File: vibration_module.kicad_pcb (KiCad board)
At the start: 2 copper layers, 17.5 x 17 mm, 21 parts, among them J1 I2C/PWR, U1 AT42QT1011-TSHR, U2 DRV2605LDGS, U3 STM32G031G8Ux, U4 TPS7A20xxxDQN

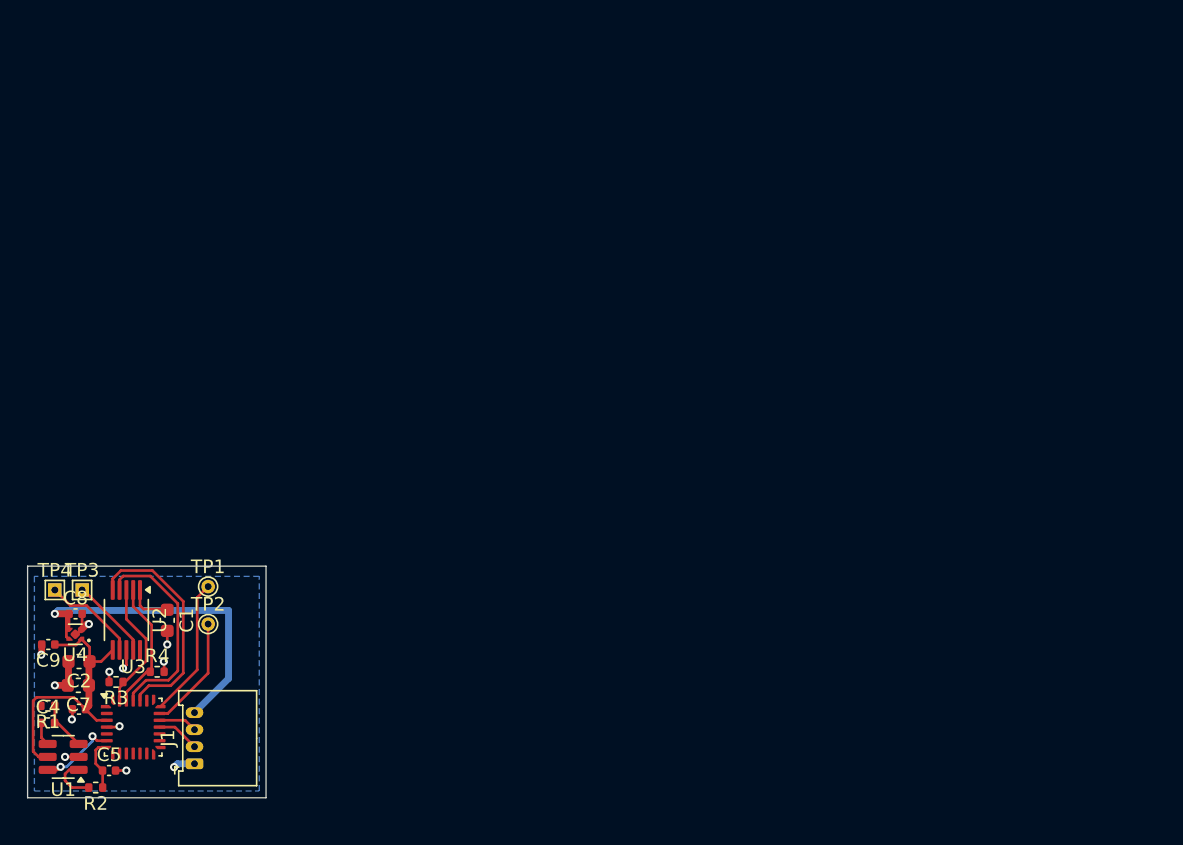
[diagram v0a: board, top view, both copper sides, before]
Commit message: mouse switch integration
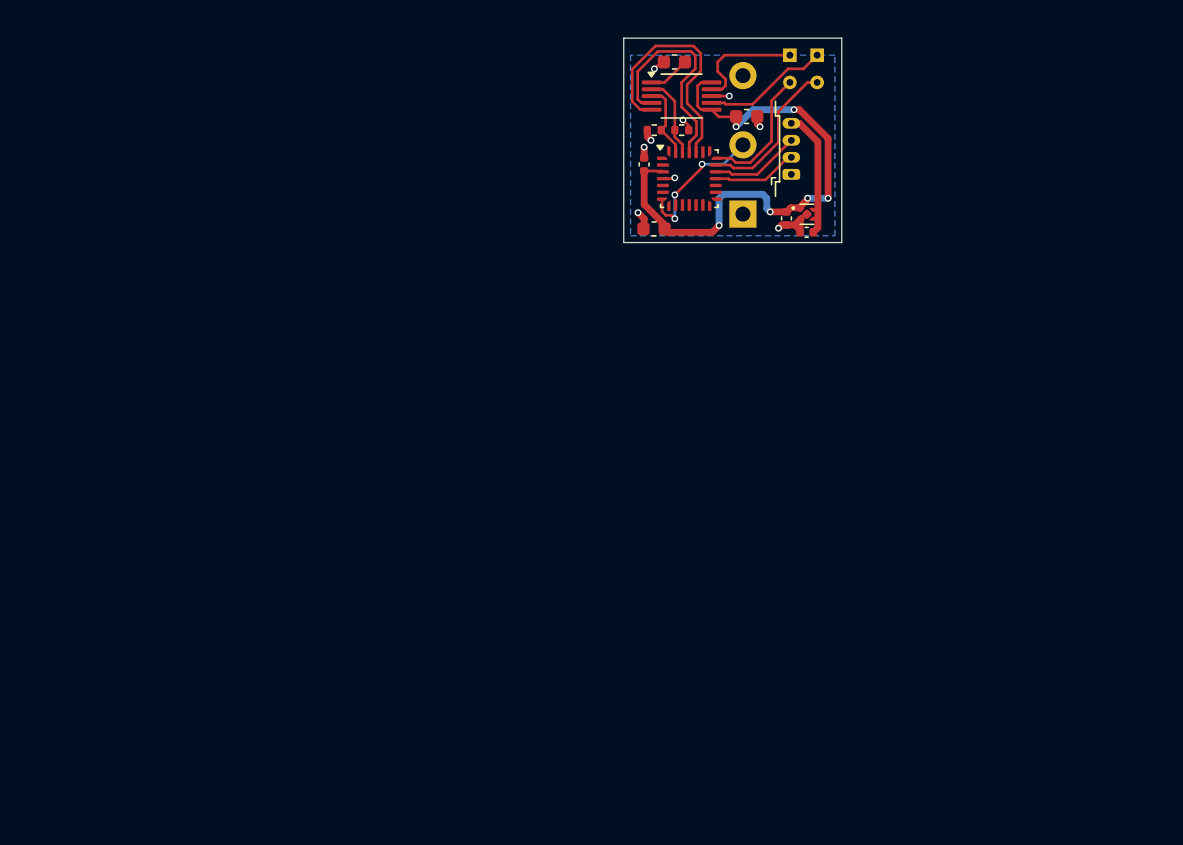
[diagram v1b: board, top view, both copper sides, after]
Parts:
- removed C4, C5: 10n, Capacitor_SMD:C_0402_1005Metric
- removed R1, R2: 10k, Resistor_SMD:R_0402_1005Metric
- removed U1: AT42QT1011-TSHR, Package_TO_SOT_SMD:SOT-23-6
- added SW1: SW_SPDT, Button_Switch_THT:SW_XKB_DM1-16UP-1, B.Cu at (163.2, 78.2)
- moved TP4 68.3 mm to (168.7, 66.5)
- moved TP3 65.1 mm to (166.7, 66.5)
- moved C2 63.3 mm to (163.5, 71.0), turned to 0 degrees
- moved C9 62.6 mm to (166.4, 78.5), turned to -90 degrees
- moved U4 61.9 mm to (167.9, 78.2), turned to 0 degrees
- moved J1 61.6 mm to (166.8, 75.2)
- moved C8 60.5 mm to (167.9, 79.5), turned to 180 degrees
- moved TP2 59.8 mm to (168.7, 68.5)
- moved C6 57.6 mm to (156.0, 74.5), turned to 90 degrees
- moved U3 57.3 mm to (159.3, 75.6)
- moved R3 56.6 mm to (156.7, 72.0)
- moved TP1 56.5 mm to (166.7, 68.5)
- moved U2 56.0 mm to (158.8, 69.5), turned to 0 degrees
- moved C1 55.4 mm to (158.2, 67.0), turned to 0 degrees
- moved R4 55.3 mm to (158.8, 72.0)
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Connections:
- U3 pad 6: Net-(U1-SYNC) -> unconnected-(U3-PA0-Pad6)
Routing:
- net +3.3V: track 21.2 -> 41.2 mm, vias 0 -> 6
- net VBUS: track 25.6 -> 8.91 mm, vias 1 -> 0
- net Net-(SW1-B): track 3.79 -> 10.5 mm, vias 0 -> 3
- net Net-(U1-SYNC): track 5.70 -> 0.00 mm, vias 2 -> 0
- net Net-(U2-SDA): track 9.53 -> 5.57 mm
- net /SDA: track 2.85 -> 6.66 mm
- net Net-(U1-SNSK): track 3.67 -> 0.00 mm
- net Net-(U1-OUT): track 3.57 -> 0.00 mm
- net Net-(U2-SCL): track 9.38 -> 6.05 mm
- net /SCL: track 3.16 -> 6.38 mm
- net Net-(U3-PA13): track 8.39 -> 11.6 mm
- net Net-(U2-OUT-): track 6.02 -> 8.61 mm
- net Net-(U2-OUT+): track 7.06 -> 9.28 mm
- net Net-(U1-SNS): track 1.74 -> 0.00 mm
- net GND: track 14.1 -> 12.4 mm, vias 11 -> 9
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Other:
- board size 17.5 x 17 mm -> 16 x 15 mm
- copper layers 2 -> 4

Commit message: change proj structure
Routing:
- net +3.3V: track 41.2 -> 42.0 mm
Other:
- copper layers 4 -> 2
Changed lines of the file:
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@@
 	(layers
 		(0 "F.Cu" signal)
-		(4 "In1.Cu" signal)
-		(6 "In2.Cu" signal)
 		(2 "B.Cu" signal)
 		(9 "F.Adhes" user "F.Adhesive")
@@
 			)
 			(layer "dielectric 1"
-				(type "prepreg")
-				(thickness 0.1)
-				(material "FR4")
-				(epsilon_r 4.5)
-				(loss_tangent 0.02)
-			)
-			(layer "In1.Cu"
-				(type "copper")
-				(thickness 0.035)
-			)
-			(layer "dielectric 2"
 				(type "core")
-				(thickness 1.24)
-				(material "FR4")
-				(epsilon_r 4.5)
-				(loss_tangent 0.02)
-			)
-			(layer "In2.Cu"
-				(type "copper")
-				(thickness 0.035)
-			)
-			(layer "dielectric 3"
-				(type "prepreg")
-				(thickness 0.1)
+				(thickness 1.51)
 				(material "FR4")
 				(epsilon_r 4.5)
@@
 	)
 	(segment
+		(start 162 71.5)
+		(end 162.5 71)
+		(width 0.5)
+		(layer "F.Cu")
+		(net 4)
+	)
+	(segment
 		(start 161.5 79)
 		(end 161 79.5)
@@
 	)
 	(segment
-		(start 162.75 71.75)
-		(end 162.75 71)
-		(width 0.5)
-		(layer "F.Cu")
-		(net 4)
-	)
-	(segment
 		(start 169.5 72.609041)
 		(end 167.390959 70.5)
@@
 	)
 	(segment
+		(start 162.5 71)
+		(end 162.75 71)
+		(width 0.5)
+		(layer "F.Cu")
+		(net 4)
+	)
+	(segment
 		(start 159.924 68.767176)
 		(end 160.191176 68.5)
@@
 	)
 	(via
-		(at 162.75 71.75)
+		(at 162 71.5)
 		(size 0.5)
 		(drill 0.3)
@@
 	)
 	(segment
-		(start 165 77.008)
-		(end 164.701 76.709)
-		(width 0.5)
-		(layer "B.Cu")
-		(net 4)
-	)
-	(segment
-		(start 168 77)
-		(end 169.5 77)
+		(start 163 70.5)
+		(end 167 70.5)
 		(width 0.5)
 		(layer "B.Cu")
@@
 	)
 	(segment
-		(start 164 70.5)
-		(end 162.75 71.75)
+		(start 165 77.008)
+		(end 164.701 76.709)
 		(width 0.5)
 		(layer "B.Cu")
@@
 	)
 	(segment
-		(start 167 70.5)
-		(end 164 70.5)
+		(start 168 77)
+		(end 169.5 77)
 		(width 0.5)
 		(layer "B.Cu")
@@
 	)
 	(segment
+		(start 162 71.5)
+		(end 163 70.5)
+		(width 0.5)
+		(layer "B.Cu")
+		(net 4)
+	)
+	(segment
 		(start 164.701 76.709)
 		(end 161.799 76.709)
@@
 	)
 	(segment
-		(start 168.75 79.156099)
-		(end 168.406099 79.5)
+		(start 167.196099 71.5)
+		(end 167.399595 71.5)
+		(width 0.5)
+		(layer "F.Cu")
+		(net 33)
+	)
+	(segment
+		(start 168.75 78.419033)
+		(end 168.376099 78.792934)
 		(width 0.5)
 		(layer "F.Cu")
@@
 	)
 	(segment
-		(start 168.75 72.850405)
-		(end 168.75 79.156099)
+		(start 168.376099 79.47)
+		(end 168.406099 79.5)
 		(width 0.5)
 		(layer "F.Cu")
@@
 	(segment
 		(start 167.399595 71.5)
-		(end 168.75 72.850405)
+		(end 168.731 72.831405)
 		(width 0.5)
 		(layer "F.Cu")
@@
 	)
 	(segment
-		(start 167.196099 71.5)
-		(end 167.399595 71.5)
+		(start 168.426412 77.607379)
+		(end 168.75 77.930967)
+		(width 0.5)
+		(layer "F.Cu")
+		(net 33)
+	)
+	(segment
+		(start 168.731 77.302791)
+		(end 168.426412 77.607379)
+		(width 0.5)
+		(layer "F.Cu")
+		(net 33)
+	)
+	(segment
+		(start 168.731 72.831405)
+		(end 168.731 77.302791)
+		(width 0.5)
+		(layer "F.Cu")
+		(net 33)
+	)
+	(segment
+		(start 168.75 77.930967)
+		(end 168.75 78.419033)
+		(width 0.5)
+		(layer "F.Cu")
+		(net 33)
+	)
+	(segment
+		(start 168.376099 78.792934)
+		(end 168.376099 79.47)
 		(width 0.5)
 		(layer "F.Cu")
@@
 		(layer "B.Cu")
 		(hatch edge 0.5)
-		(connect_pads
+		(connect_pads yes
 			(clearance 0.5)
 		)

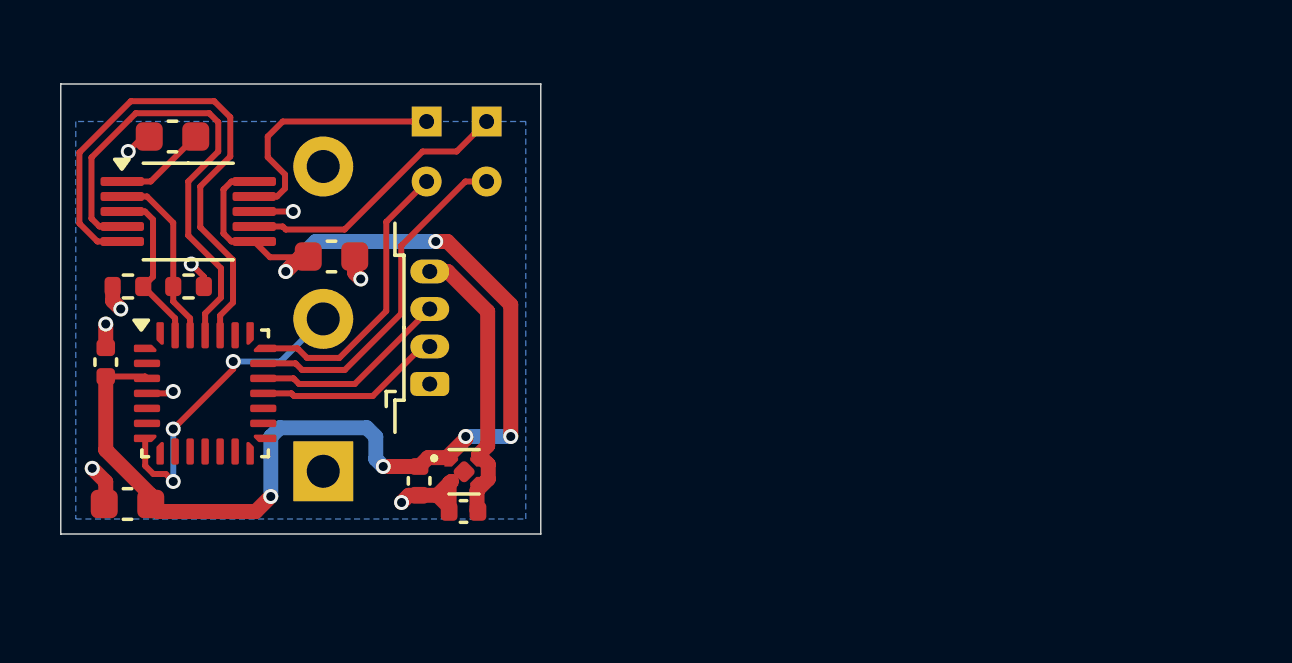
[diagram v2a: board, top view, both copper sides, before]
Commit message: keyboard version poc
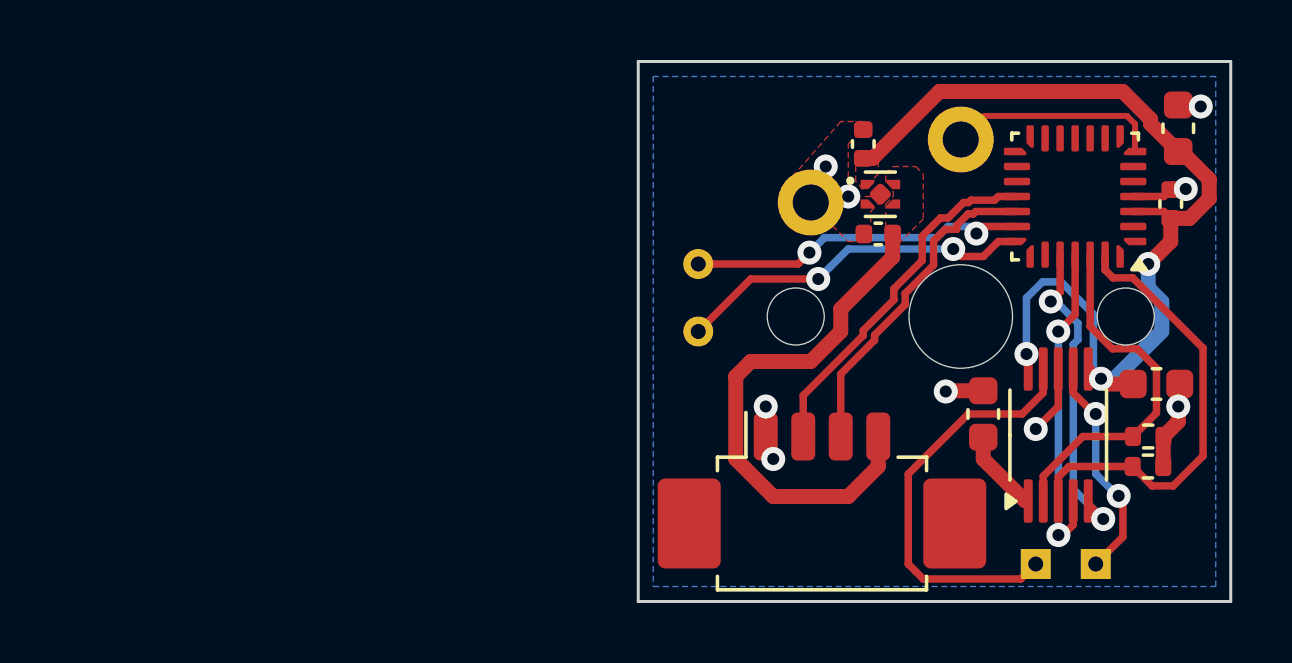
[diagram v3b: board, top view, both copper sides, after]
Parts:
- removed SW1: SW_SPDT, Button_Switch_THT:SW_XKB_DM1-16UP-1
- added SW2: SW_SPST, PCM_Switch_Keyboard_Kailh:SW_Kailh_Choc_V1_1.00u, B.Cu at (184.5, 73.0)
- J1: footprint Connector_Molex:Molex_PicoBlade_53048-0410_1x04_P1.25mm_Horizontal -> Connector_Molex:Molex_PicoBlade_53261-0471_1x04-1MP_P1.25mm_Horizontal
- moved C7 37.2 mm to (191.8, 66.7), turned to 90 degrees
- moved C6 35.9 mm to (191.5, 69.2)
- moved R3 34.5 mm to (190.7, 78.0), turned to 0 degrees
- moved R4 32.4 mm to (190.8, 77.0)
- moved U2 29.9 mm to (187.8, 77.0), turned to 90 degrees
- moved U3 29.7 mm to (188.3, 69.0), turned to 180 degrees
- moved C1 28.6 mm to (185.2, 76.2), turned to -90 degrees
- moved C2 27.8 mm to (191.0, 75.2)
- moved TP3 25.1 mm to (187.0, 81.2)
- moved TP4 25.1 mm to (189.0, 81.2)
- moved C9 18.6 mm to (181.2, 67.2), turned to 90 degrees
- moved U4 16.7 mm to (181.8, 68.9)
- moved C8 16.6 mm to (181.8, 70.2)
- moved J1 13.7 mm to (179.9, 79.4), turned to 0 degrees
- moved TP1 10.3 mm to (175.8, 73.5)
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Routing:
- net Net-(U2-SDA): track 5.57 -> 14.9 mm
- net +3.3V: track 42.0 -> 33.5 mm, vias 6 -> 3
- net VBUS: track 9.18 -> 17.5 mm
- net Net-(U2-EN): track 18.3 -> 10.7 mm, vias 0 -> 2
- net Net-(U2-SCL): track 6.05 -> 12.2 mm
- net /SCL: track 6.38 -> 12.0 mm
- net Net-(U2-OUT-): track 8.61 -> 14.1 mm
- net Net-(U2-IN/TRIG): track 16.3 -> 11.0 mm, vias 0 -> 2
- net /SDA: track 6.66 -> 11.1 mm
- net Net-(SW2-A): track 10.5 -> 7.16 mm, vias 3 -> 0
- net Net-(U3-PA14): track 9.70 -> 12.0 mm, vias 0 -> 2
- net Net-(U2-OUT+): track 9.28 -> 7.61 mm, vias 0 -> 2
- net GND: track 12.4 -> 11.0 mm
- net Net-(U3-PA13): track 11.6 -> 11.3 mm, vias 0 -> 2
- added copper zone on F.Cu, net +3.3V
- added copper zone on F.Cu, net GND
- added copper zone on F.Cu, net VBUS
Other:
- board size 16 x 15 mm -> 19.8 x 18 mm
